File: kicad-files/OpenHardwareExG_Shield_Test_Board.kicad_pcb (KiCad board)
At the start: 4 copper layers, 125.1 x 59.7 mm, 56 parts, among them P1 CONN_1, P11 CONN_1, P12 CONN_1, P13 CONN_1, P14 CONN_1, P15 CONN_1, P16 CONN_1, P17 CONN_1, P18 CONN_1, P2 CONN_1, P23 CONN_1, P24 CONN_1, P25 CONN_1, P26 CONN_1, P27 CONN_1, P28 CONN_1, P29 CONN_1, P3 CONN_1, P30 CONN_1, P31 CONN_1, P32 CONN_1, P33 CONN_1, P34 CONN_1, P35 CONN_1, P36 CONN_1, P37 CONN_1, P38 CONN_1, P39 CONN_1, P4 CONN_1, P40 CONN_1, P41 CONN_1, P42 CONN_1, P43 CONN_1, P44 CONN_1, P45 CONN_1, P46 CONN_1, P47 CONN_1, P48 CONN_1, P49 CONN_1, P5 CONN_1, P50 CONN_1, P51 CONN_1, P52 CONN_1, P53 CONN_1, P54 CONN_1, P55 CONN_1, P6 CONN_1, P7 CONN_1, P8 CONN_1, P9 CONN_1

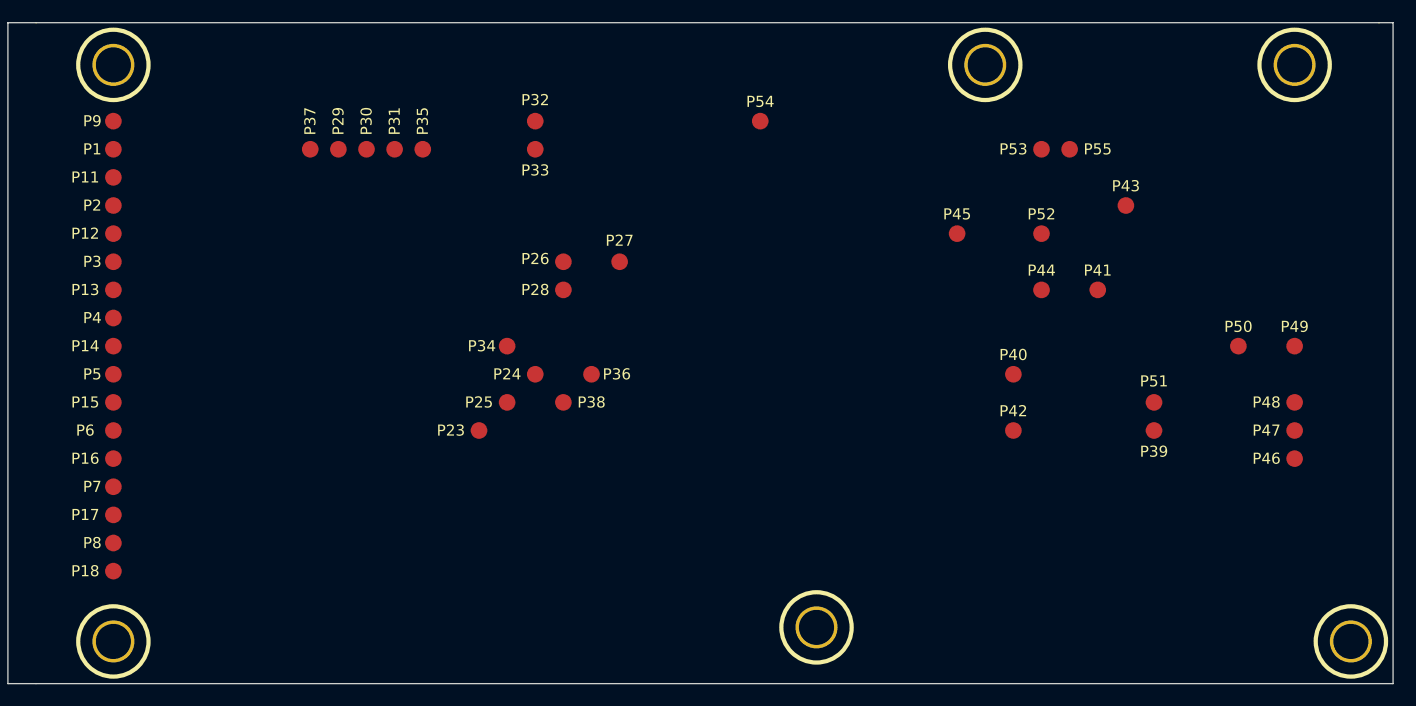
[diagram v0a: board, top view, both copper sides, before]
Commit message: swap-in pogo-pins for pads
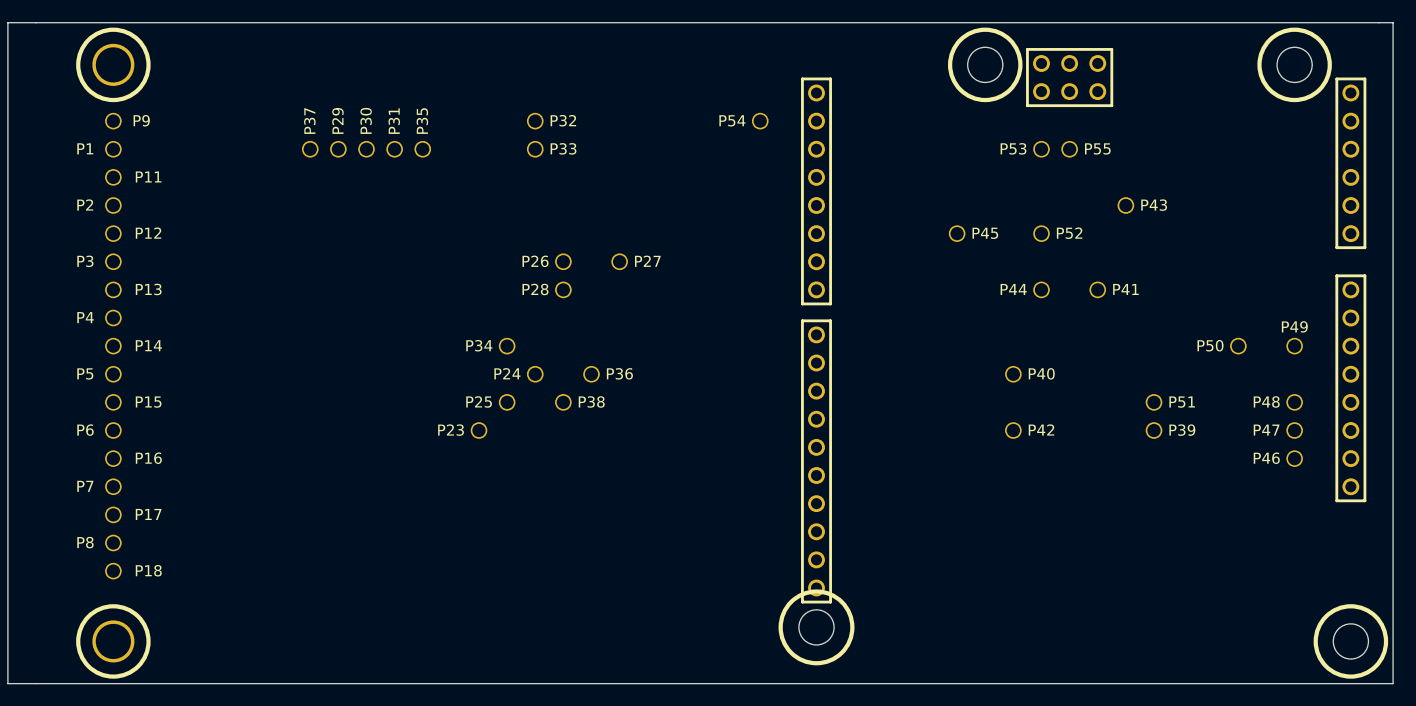
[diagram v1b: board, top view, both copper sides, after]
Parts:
- removed the Hole_M3 at (132.1, 83.8)
- removed the Hole_M3 at (175.3, 33.0)
- removed the Hole_M3 at (180.3, 85.1)
- removed the Hole_M3 at (147.3, 33.0)
- added arduino_shield_with_holes: VAL**, arduino_shield_with_holes, F.Cu at (154.9, 54.6)
- P1, P11, P12, P13, P14, P15, P16, P17, P18, P2, P23, P24, P25, P26, P27, P28, P29, P3, P30, P31, P32, P33, P34, P35, P36, P37, P38, P39, P4, P40, P41, P42, P43, P44, P45, P46, P47, P48, P49, P5, P50, P51, P52, P53, P54, P55, P6, P7, P8, P9: footprint POGO_PAD -> POGO_PIN_BASE

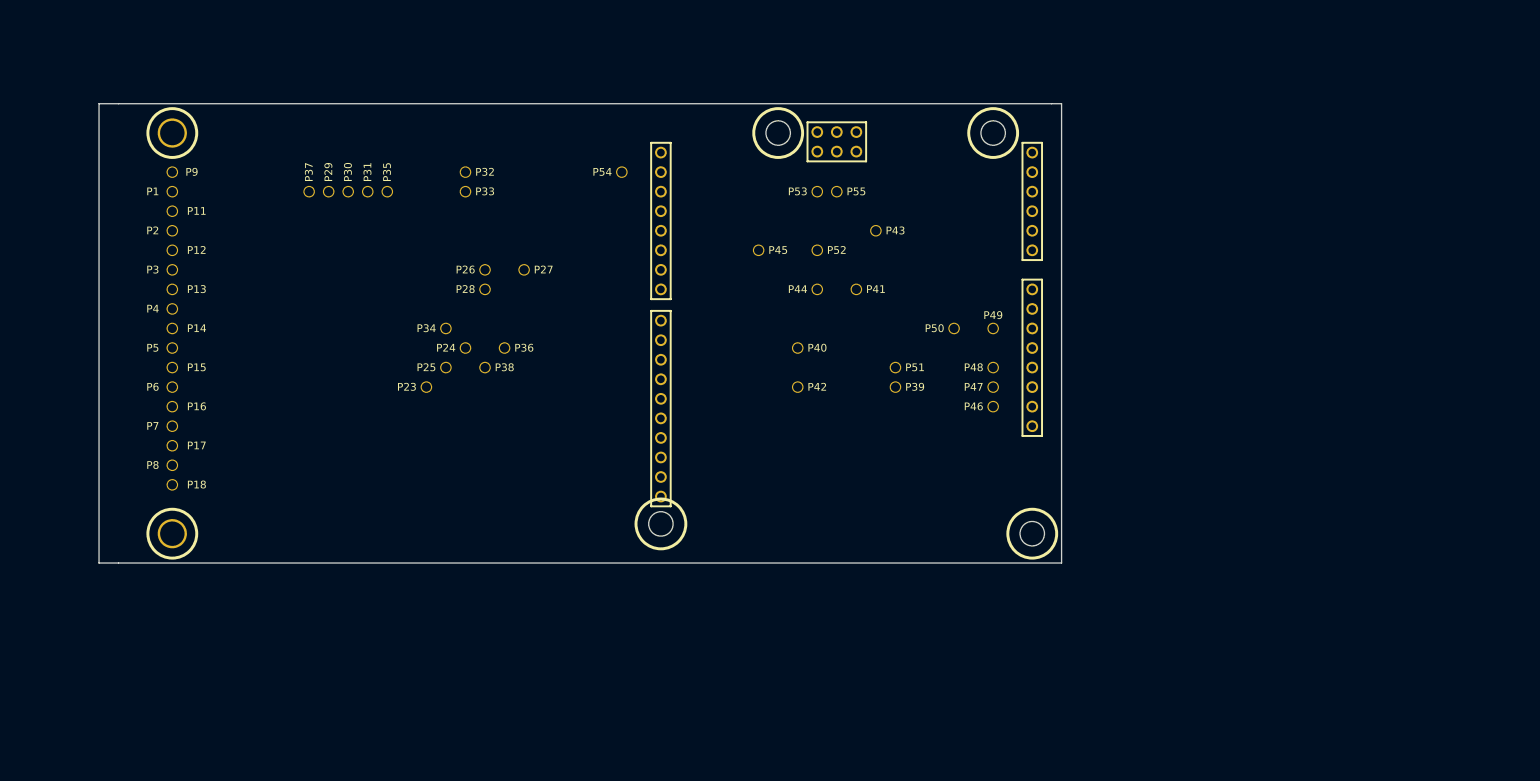
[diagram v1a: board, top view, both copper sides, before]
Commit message: checkpoint tesh-harness pcb, components separated
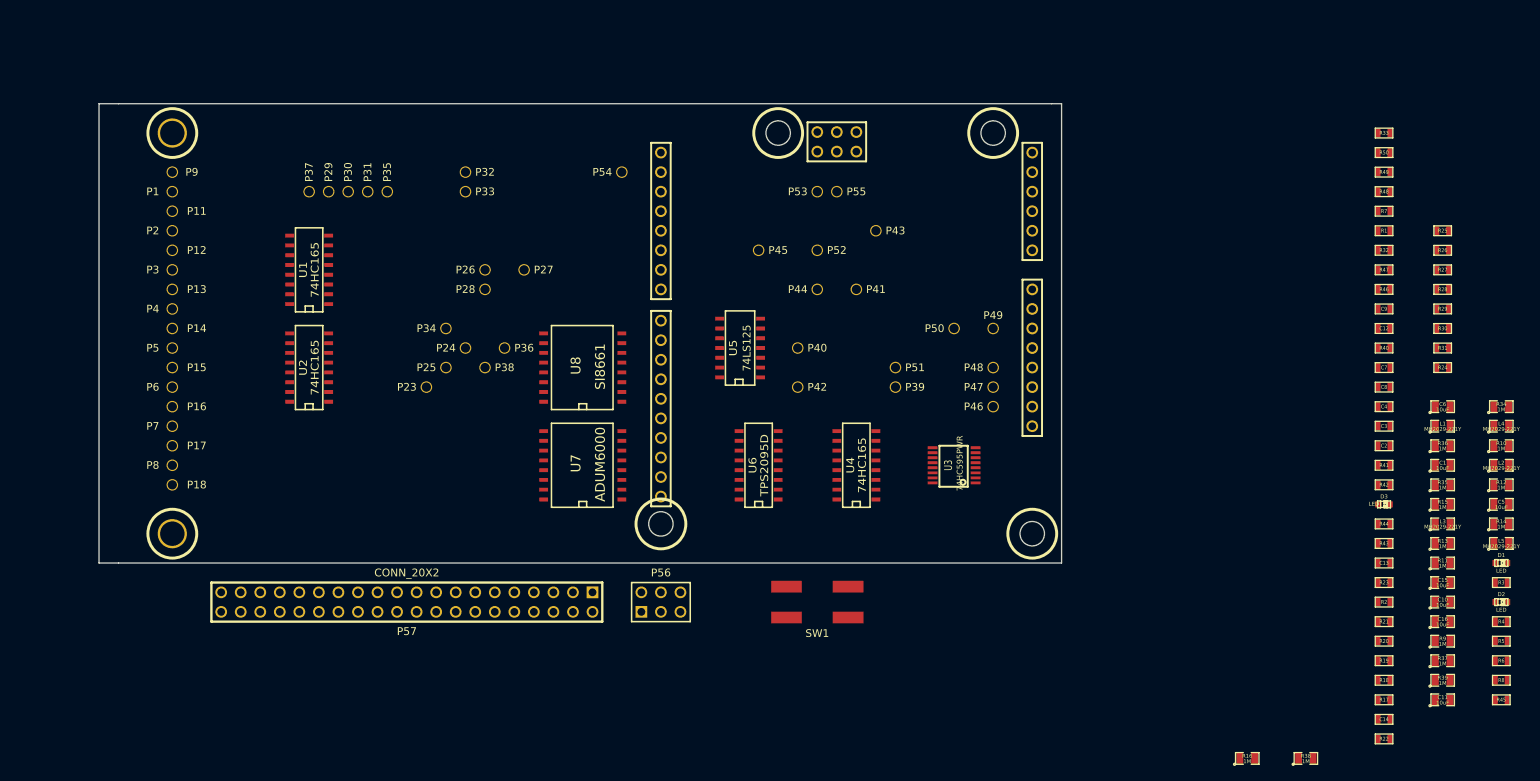
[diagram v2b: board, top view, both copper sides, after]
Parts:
- added C1: 10uF, SM0805, F.Cu at (233.7, 76.2)
- added C10: 10uF, SM0805, F.Cu at (233.7, 94.0)
- added C11: 10uF, SM0805, F.Cu at (233.7, 106.7)
- added C12: 100nF, SM0603, F.Cu at (226.1, 58.4)
- added C13: 100nF, SM0603, F.Cu at (226.1, 88.9)
- added C14: 100nF, SM0603, F.Cu at (226.1, 109.2)
- added C15: 10uF, SM0805, F.Cu at (233.7, 91.4)
- added C16: 10uF, SM0805, F.Cu at (233.7, 96.5)
- added C2: 100nF, SM0603, F.Cu at (226.1, 73.7)
- added C3: 100nF, SM0603, F.Cu at (226.1, 71.1)
- added C4: 100nF, SM0603, F.Cu at (226.1, 68.6)
- added C5: 10uF, SM0805, F.Cu at (241.3, 81.3)
- added C6: 10uF, SM0805, F.Cu at (233.7, 68.6)
- added C7: 100nF, SM0603, F.Cu at (226.1, 63.5)
- added C8: 100nF, SM0603, F.Cu at (226.1, 66.0)
- added C9: 100nF, SM0603, F.Cu at (226.1, 55.9)
- added D1: LED, LED-0603, F.Cu at (241.3, 88.9)
- added D2: LED, LED-0603, F.Cu at (241.3, 94.0)
- added D3: LED, LED-0603, F.Cu at (226.1, 81.3)
- added L1: MH2029-221Y, SM0805, F.Cu at (233.7, 71.1)
- added L2: MH2029-221Y, SM0805, F.Cu at (241.3, 76.2)
- added L3: MH2029-221Y, SM0805, F.Cu at (233.7, 83.8)
- added L4: MH2029-221Y, SM0805, F.Cu at (241.3, 71.1)
- added L5: MH2029-221Y, SM0805, F.Cu at (241.3, 86.4)
- added P56: CONN_3X2, pin_array_3x2, F.Cu at (132.1, 94.0)
- added P57: CONN_20X2, PIN_ARRAY_20X2, F.Cu at (99.1, 94.0)
- added R1: 10k, SM0603, F.Cu at (226.1, 45.7)
- added R10: 1M, SM0805, F.Cu at (241.3, 73.7)
- added R11: 1M, SM0805, F.Cu at (233.7, 88.9)
- added R12: 1M, SM0805, F.Cu at (241.3, 78.7)
- added R13: 1M, SM0805, F.Cu at (233.7, 86.4)
- added R14: 1M, SM0805, F.Cu at (241.3, 83.8)
- added R15: 1M, SM0805, F.Cu at (233.7, 81.3)
- added R16: 1M, SM0805, F.Cu at (208.3, 114.3)
- added R17: 15k, SM0603, F.Cu at (226.1, 106.7)
- added R18: 100, SM0603, F.Cu at (226.1, 104.1)
- added R19: 100, SM0603, F.Cu at (226.1, 101.6)
- added R2: 1k, SM0603, F.Cu at (226.1, 94.0)
- added R20: 100, SM0603, F.Cu at (226.1, 99.1)
- added R21: 100, SM0603, F.Cu at (226.1, 96.5)
- added R22: 100, SM0603, F.Cu at (226.1, 111.8)
- added R23: 100, SM0603, F.Cu at (226.1, 91.4)
- added R24: 100, SM0603, F.Cu at (233.7, 63.5)
- added R25: 100, SM0603, F.Cu at (233.7, 45.7)
- added R26: 100, SM0603, F.Cu at (233.7, 48.3)
- added R27: 100, SM0603, F.Cu at (233.7, 50.8)
- added R28: 100, SM0603, F.Cu at (233.7, 53.3)
- added R29: 100, SM0603, F.Cu at (233.7, 55.9)
- added R3: 10k, SM0603, F.Cu at (241.3, 91.4)
- added R30: 100, SM0603, F.Cu at (233.7, 58.4)
- added R31: 100, SM0603, F.Cu at (233.7, 61.0)
- added R32: 100, SM0603, F.Cu at (226.1, 48.3)
- added R33: 15k, SM0603, F.Cu at (226.1, 33.0)
- added R34: 1M, SM0805, F.Cu at (241.3, 68.6)
- added R35: 1M, SM0805, F.Cu at (233.7, 78.7)
- added R36: 1M, SM0805, F.Cu at (233.7, 73.7)
- added R37: 1M, SM0805, F.Cu at (233.7, 101.6)
- added R38: 1M, SM0805, F.Cu at (215.9, 114.3)
- added R39: 1M, SM0805, F.Cu at (233.7, 104.1)
- added R4: 1k, SM0603, F.Cu at (241.3, 96.5)
- added R40: 560, SM0603, F.Cu at (226.1, 61.0)
- added R41: 560, SM0603, F.Cu at (226.1, 76.2)
- added R42: 560, SM0603, F.Cu at (226.1, 78.7)
- added R43: 10k, SM0603, F.Cu at (226.1, 86.4)
- added R44: 10k, SM0603, F.Cu at (226.1, 83.8)
- added R45: 47, SM0603, F.Cu at (241.3, 106.7)
- added R46: 47, SM0603, F.Cu at (226.1, 53.3)
- added R47: 47, SM0603, F.Cu at (226.1, 50.8)
- added R48: 47, SM0603, F.Cu at (226.1, 40.6)
- added R49: 47, SM0603, F.Cu at (226.1, 38.1)
- added R5: 10k, SM0603, F.Cu at (241.3, 99.1)
- added R50: 47, SM0603, F.Cu at (226.1, 35.6)
- added R6: 1k, SM0603, F.Cu at (241.3, 101.6)
- added R7: 5.1K, SM0603, F.Cu at (226.1, 43.2)
- added R8: 100, SM0603, F.Cu at (241.3, 104.1)
- added R9: 1M, SM0805, F.Cu at (233.7, 99.1)
- added SW1: SW_PUSH, smt-tactile-button, F.Cu at (152.4, 94.0)
- added U1: 74HC165, SO16E, F.Cu at (86.4, 50.8)
- added U2: 74HC165, SO16E, F.Cu at (86.4, 63.5)
- added U3: 74HC595PWR, TSSOP16, F.Cu at (170.2, 76.2)
- added U4: 74HC165, SO16E, F.Cu at (157.5, 76.2)
- added U5: 74LS125, SO14E, F.Cu at (142.2, 61.0)
- added U6: TPS2095D, SO16E, F.Cu at (144.8, 76.2)
- added U7: ADUM6000, SO16W, F.Cu at (121.9, 76.2)
- added U8: SI8661, SO16W, F.Cu at (121.9, 63.5)
- P19: renamed from arduino_shield_with_holes; value VAL** -> ARDUINO_SHIELD
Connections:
- P19 pad 2: (no net) -> /MASTER_~DRDY~
- P19 pad 3: (no net) -> /SHIFT_OUT_~SRCLR~
- P19 pad 4: (no net) -> /SHIFT_OUT_SRCLK
- P19 pad 5: (no net) -> /SHIFT_OUT_RCLK
- P19 pad 54: (no net) -> /SHIFT_IN
- P19 pad 55: (no net) -> N-0000018
- P19 pad 56: (no net) -> N-0000019
- P19 pad 57: (no net) -> N-000002
- P19 pad 58: (no net) -> N-000004
- P19 pad 59: (no net) -> /BIASOUT_FILT
- P19 pad 6: (no net) -> /SHIFT_OUT
- P19 pad 7: (no net) -> /~SHIELD_SHORTED~
- P19 pad 74: (no net) -> /MISO
- P19 pad 75: (no net) -> /MOSI
- P19 pad 76: (no net) -> /SCLK
- P19 pad 8: (no net) -> /SHIFT_CLK
- P19 pad 87: (no net) -> GNDPWR
- P19 pad 88: (no net) -> +5V
- P19 pad 9: (no net) -> /SHIFT_SH_~LD~
- P19 pad 91: (no net) -> /ARDUINO_VCC
- P19 pad 93: (no net) -> +3.3V
- P19 pad 94: (no net) -> +5V
- P19 pad 95: (no net) -> GNDPWR
- P19 pad 96: (no net) -> GNDPWR
- P19 pad 99: (no net) -> GNDPWR
- P23 pad 1: /ADS129x_MOSI_ISO -> /ADS129x_MOSI_BOGUS_ISO
- P24 pad 1: /ADS129x_SCLK_ISO -> /ADS129x_SCLK_BOGUS_ISO
- P25 pad 1: /ADS129x_~CS~_ISO -> /ADS129x_~CS~_BOGUS_ISO
- P26 pad 1: /MASTER_ISO -> /MASTER_BOGUS_ISO
- P27 pad 1: /ADS129x_DOUT_ISO -> /ADS129x_DOUT_BOGUS_ISO
- P28 pad 1: /ADS129x_~DRDY~_ISO -> /ADS129x_~DRDY~_BOGUS_ISO
- P29 pad 1: /VIN_ISO -> /VIN_BOGUS_ISO
- P30 pad 1: /3.3V_ISO -> /3.3V_BOGUS_ISO
- P31 pad 1: /DGND_ISO -> /DGND_BOGUS_ISO
- P32 pad 1: /ADS129x_GPIO1_ISO -> /ADS129x_GPIO1_BOGUS_ISO
- P33 pad 1: /ADS129x_GPIO2_ISO -> /ADS129x_GPIO2_BOGUS_ISO
- P34 pad 1: /ADS129x_GPIO3_ISO -> /ADS129x_GPIO3_BOGUS_ISO
- P35 pad 1: /ADS129x_GPIO4_ISO -> /ADS129x_GPIO4_BOGUS_ISO
- P36 pad 1: /ADS129x_DAISY_IN_ISO -> /ADS129x_DAISY_IN_BOGUS_ISO
- P38 pad 1: /ADS129x_CLK_ISO -> /ADS129x_CLK_BOGUS_ISO
- P46 pad 1: /ARDUINO_VCC -> /SHIELD_VCC
- P47 pad 1: +3.3V -> /SHIELD_3.3V
- P48 pad 1: +5V -> /SHIELD_5V
- P49 pad 1: GND -> GNDPWR

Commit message: re-order signal ladder for easier physical layout
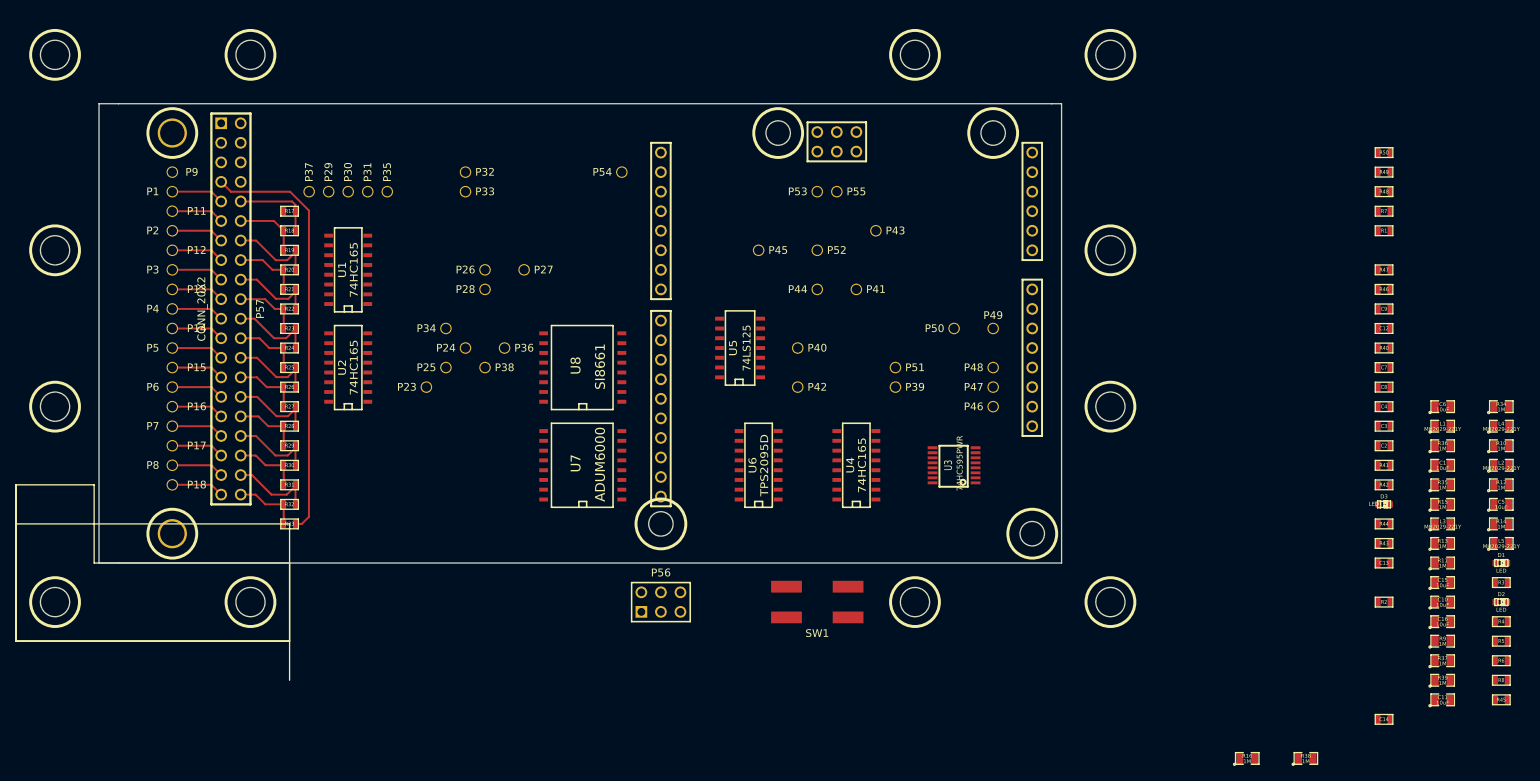
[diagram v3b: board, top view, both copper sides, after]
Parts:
- added Hole_M3: VAL**, Hole_M3, F.Cu at (165.1, 94.0)
- added Hole_M3: VAL**, Hole_M3, F.Cu at (53.3, 68.6)
- added Hole_M3: VAL**, Hole_M3, F.Cu at (53.3, 48.3)
- added Hole_M3: VAL**, Hole_M3, F.Cu at (190.5, 48.3)
- added Hole_M3: VAL**, Hole_M3, F.Cu at (190.5, 68.6)
- added Hole_M3: VAL**, Hole_M3, F.Cu at (190.5, 22.9)
- added Hole_M3: VAL**, Hole_M3, F.Cu at (165.1, 22.9)
- added Hole_M3: VAL**, Hole_M3, F.Cu at (78.7, 22.9)
- added Hole_M3: VAL**, Hole_M3, F.Cu at (53.3, 22.9)
- added Hole_M3: VAL**, Hole_M3, F.Cu at (53.3, 94.0)
- added Hole_M3: VAL**, Hole_M3, F.Cu at (78.7, 94.0)
- added Hole_M3: VAL**, Hole_M3, F.Cu at (190.5, 94.0)
- moved R17 155.8 mm to (83.8, 43.2)
- moved R18 153.8 mm to (83.8, 45.7)
- moved R22 152.8 mm to (83.8, 55.9)
- moved R19 151.9 mm to (83.8, 48.3)
- moved R33 151.0 mm to (83.8, 83.8)
- moved R25 150.9 mm to (83.8, 63.5)
- moved R26 150.9 mm to (83.8, 66.0)
- moved R27 150.9 mm to (83.8, 68.6)
- moved R28 150.9 mm to (83.8, 71.1)
- moved R29 150.9 mm to (83.8, 73.7)
- moved R30 150.9 mm to (83.8, 76.2)
- moved R31 150.9 mm to (83.8, 78.7)
- moved R20 150.2 mm to (83.8, 50.8)
- moved R24 149.9 mm to (83.8, 61.0)
- moved R21 148.6 mm to (83.8, 53.3)
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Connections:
- P57 pad 10: /IN8P -> /IN8N_LADDER
- P57 pad 11: /IN8N_LADDER -> /IN8P
- P57 pad 12: /IN8N -> /IN8P_LADDER
- P57 pad 13: /IN7P_LADDER -> /IN7N
- P57 pad 14: /IN7P -> /IN7N_LADDER
- P57 pad 15: /IN7N_LADDER -> /IN7P
- P57 pad 16: /IN7N -> /IN7P_LADDER
- P57 pad 17: /IN6P_LADDER -> /IN6N
- P57 pad 18: /IN6P -> /IN6N_LADDER
- P57 pad 19: /IN6N_LADDER -> /IN6P
- P57 pad 20: /IN6N -> /IN6P_LADDER
- P57 pad 21: /IN5P_LADDER -> /IN5N
- P57 pad 22: /IN5P -> /IN5N_LADDER
- P57 pad 23: /IN5N_LADDER -> /IN5P
- P57 pad 24: /IN5N -> /IN5P_LADDER
- P57 pad 25: /IN4P_LADDER -> /IN4N
- P57 pad 26: /IN4P -> /IN4N_LADDER
- P57 pad 27: /IN4N_LADDER -> /IN4P
- P57 pad 28: /IN4N -> /IN4P_LADDER
- P57 pad 29: /IN3P_LADDER -> /IN3N
- P57 pad 30: /IN3P -> /IN3N_LADDER
- P57 pad 31: /IN3N_LADDER -> /IN3P
- P57 pad 32: /IN3N -> /IN3P_LADDER
- P57 pad 33: /IN2P_LADDER -> /IN2N
- P57 pad 34: /IN2P -> /IN2N_LADDER
- P57 pad 35: /IN2N_LADDER -> /IN2P
- P57 pad 36: /IN2N -> /IN2P_LADDER
- P57 pad 37: /IN1P_LADDER -> /IN1N
- P57 pad 38: /IN1P -> /IN1N_LADDER
- P57 pad 39: /IN1N_LADDER -> /IN1P
- P57 pad 40: /IN1N -> /IN1P_LADDER
- P57 pad 9: /IN8P_LADDER -> /IN8N
- R17 pad 2: /IN8P_LADDER -> /IN8N_LADDER
- R18 pad 1: /IN8N_LADDER -> /IN8P_LADDER
- R18 pad 2: /IN8P_LADDER -> /IN8N_LADDER
- R19 pad 1: /IN8N_LADDER -> /IN8P_LADDER
- R19 pad 2: /IN7P_LADDER -> /IN7N_LADDER
- R20 pad 1: /IN7N_LADDER -> /IN7P_LADDER
- R20 pad 2: /IN7P_LADDER -> /IN7N_LADDER
- R21 pad 1: /IN7N_LADDER -> /IN7P_LADDER
- R21 pad 2: /IN6P_LADDER -> /IN6N_LADDER
- R22 pad 1: /IN6N_LADDER -> /IN6P_LADDER
- R22 pad 2: /IN6P_LADDER -> /IN6N_LADDER
- R23 pad 1: /IN6N_LADDER -> /IN6P_LADDER
- R23 pad 2: /IN5P_LADDER -> /IN5N_LADDER
- R24 pad 1: /IN5N_LADDER -> /IN5P_LADDER
- R24 pad 2: /IN5P_LADDER -> /IN5N_LADDER
- R25 pad 1: /IN5N_LADDER -> /IN5P_LADDER
- R25 pad 2: /IN4P_LADDER -> /IN4N_LADDER
- R26 pad 1: /IN4N_LADDER -> /IN4P_LADDER
- R26 pad 2: /IN4P_LADDER -> /IN4N_LADDER
- R27 pad 1: /IN4N_LADDER -> /IN4P_LADDER
- R27 pad 2: /IN3P_LADDER -> /IN3N_LADDER
- R28 pad 1: /IN3N_LADDER -> /IN3P_LADDER
- R28 pad 2: /IN3P_LADDER -> /IN3N_LADDER
- R29 pad 1: /IN3N_LADDER -> /IN3P_LADDER
- R29 pad 2: /IN2P_LADDER -> /IN2N_LADDER
- R30 pad 1: /IN2N_LADDER -> /IN2P_LADDER
- R30 pad 2: /IN2P_LADDER -> /IN2N_LADDER
- R31 pad 1: /IN2N_LADDER -> /IN2P_LADDER
- R31 pad 2: /IN1P_LADDER -> /IN1N_LADDER
- R32 pad 1: /IN1N_LADDER -> /IN1P_LADDER
- R32 pad 2: /IN1P_LADDER -> /IN1N_LADDER
- R33 pad 1: /IN1N_LADDER -> /IN1P_LADDER
- U7 pad 14: (no net) -> GND
- U7 pad 3: (no net) -> GNDPWR
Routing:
- net /SIGNAL_B_LADDER: track 0.00 -> 54.9 mm
- net /IN2N_LADDER: track 0.00 -> 11.4 mm
- net /IN7N_LADDER: track 0.00 -> 11.4 mm
- net /IN3N_LADDER: track 0.00 -> 11.4 mm
- net /IN6N_LADDER: track 0.00 -> 11.4 mm
- net /IN4N_LADDER: track 0.00 -> 11.3 mm
- net /IN1N_LADDER: track 0.00 -> 11.3 mm
- net /IN5N_LADDER: track 0.00 -> 11.3 mm
- net /IN8N_LADDER: track 0.00 -> 10.7 mm
- net /IN6P_LADDER: track 0.00 -> 8.65 mm
- net /IN5P_LADDER: track 0.00 -> 8.65 mm
- net /IN7P_LADDER: track 0.00 -> 8.65 mm
- net /IN4P_LADDER: track 0.00 -> 8.65 mm
- net /IN3P_LADDER: track 0.00 -> 8.65 mm
- net /IN8P_LADDER: track 0.00 -> 8.65 mm
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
